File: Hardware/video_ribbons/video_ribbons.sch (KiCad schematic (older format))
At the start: 33 parts, among them J1 Conn_Coaxial_Sleeve_Pin2Tip, J2 Conn_01x02, U1 74HC138, U15 74HC00, U2 74HC02, U23 74HC02, U3 74HC00, U4 IDT7130, U5 74HC08, U6 74HC86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

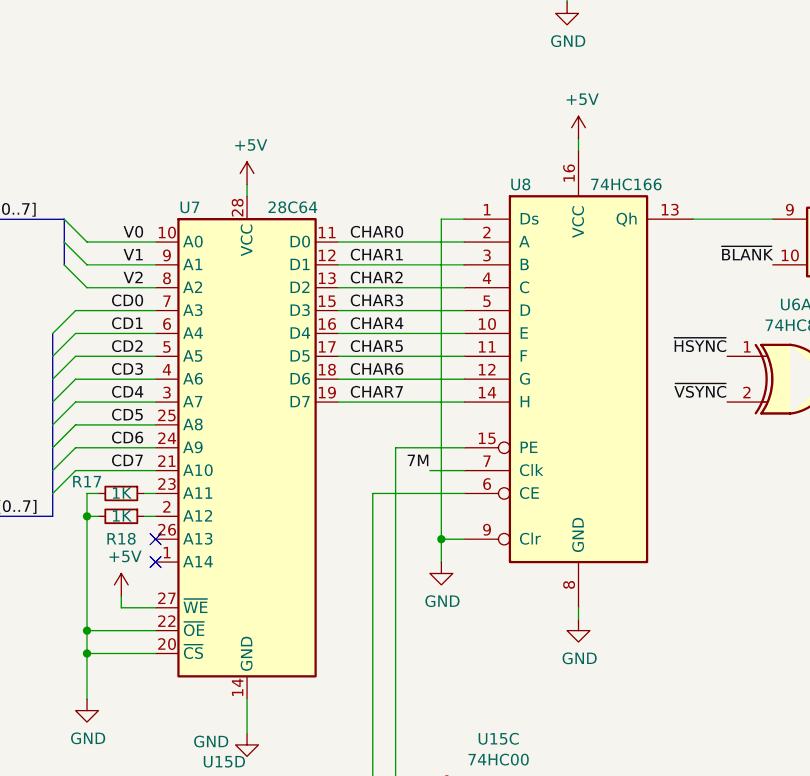
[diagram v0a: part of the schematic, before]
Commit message: Fix video clear line
Resolves #5.
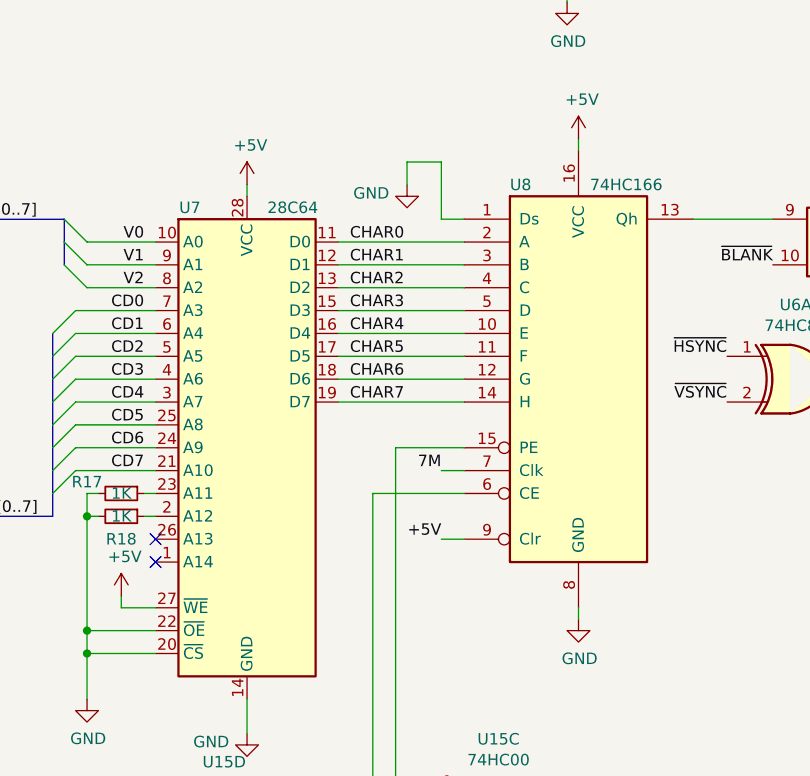
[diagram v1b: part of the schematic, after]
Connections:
- net +5V: now also U8.9 (Clr)
- net GND: no longer U8.9 (Clr)
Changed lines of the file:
@@
 Sheet 1 5
 Title "74 Character Generator (Ribbon cable)"
-Date "2021-07-29"
-Rev "1"
+Date "2021-12-24"
+Rev "2"
 Comp "rjh"
 Comment1 "CC-BY-SA 4.0"
@@
 Wire Wire Line
 	7200 4400 7200 5700
-Text Label 7450 4300 2    50   ~ 0
+Text Label 7500 4300 2    50   ~ 0
 7M
 $Sheet
@@
 L power:GND #PWR016
 U 1 1 6126EBB8
-P 7500 4700
-F 0 "#PWR016" H 7500 4450 50  0001 C CNN
-F 1 "GND" H 7505 4527 50  0000 C CNN
-F 2 "" H 7500 4700 50  0001 C CNN
-F 3 "" H 7500 4700 50  0001 C CNN
-	1    7500 4700
-	1    0    0    -1
-$EndComp
-Wire Wire Line
-	7600 4600 7500 4600
-Wire Wire Line
-	7500 4600 7500 4700
-Wire Wire Line
-	7500 4600 7500 3200
+P 7350 3050
+F 0 "#PWR016" H 7350 2800 50  0001 C CNN
+F 1 "GND" H 7272 3013 50  0000 R CNN
+F 2 "" H 7350 3050 50  0001 C CNN
+F 3 "" H 7350 3050 50  0001 C CNN
+	1    7350 3050
+	1    0    0    -1
+$EndComp
 Wire Wire Line
 	7500 3200 7600 3200
-Connection ~ 7500 4600
-Wire Wire Line
-	7450 4300 7600 4300
+Wire Wire Line
+	7500 4300 7600 4300
 $Comp
 L power:GND #PWR021
@@
 Wire Wire Line
 	6000 4500 5950 4500
+Text Label 7500 4600 2    50   ~ 0
++5V
+Wire Wire Line
+	7500 3200 7500 2950
+Wire Wire Line
+	7500 2950 7350 2950
+Wire Wire Line
+	7350 2950 7350 3050
+Wire Wire Line
+	7500 4600 7600 4600
 Wire Bus Line
 	3550 2800 3550 3000
